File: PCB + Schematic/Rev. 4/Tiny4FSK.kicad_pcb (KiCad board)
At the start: 4 copper layers, 18.5 x 64 mm, 80 parts, among them IC1 SI4063, J1 SWD, J2 GPIO, J3 USBC, J4 USB, J5 I2C, J6 Power, J7 SPI, J8 USB, SW1 RST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

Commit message: Add ATGM336H, start snap-off boards
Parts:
- added C28: 10uF, Capacitor_SMD:C_0805_2012Metric_Pad1.18x1.45mm_HandSolder, F.Cu at (145.2, 56.2)
- added R14: 1M, Resistor_SMD:R_0805_2012Metric_Pad1.20x1.40mm_HandSolder, F.Cu at (146.0, 71.8)
- added R15: 1M, Resistor_SMD:R_0805_2012Metric_Pad1.20x1.40mm_HandSolder, F.Cu at (145.8, 74.8)
- U2: value MAX-M10S -> ATGM336H; footprint RF_GPS:ublox_MAX -> RF_GPS_Extended:ATGM336H
- moved R7 53.1 mm to (165.2, 54.1)
- moved R3 50.6 mm to (162.1, 55.0), turned to -90 degrees
- moved R5 49.8 mm to (164.9, 56.0)
- moved J5 48.1 mm to (162.8, 82.7)
- moved J8 45.9 mm to (162.9, 65.8), turned to 90 degrees
- moved C15 45.7 mm to (145.2, 60.2), turned to 90 degrees
- moved BT1 43.1 mm to (214.2, 41.5)
- moved U3 42.0 mm to (164.4, 60.0), turned to 180 degrees
- moved FB1 38.3 mm to (171.2, 61.5), turned to 90 degrees
- moved J3 34.1 mm to (166.5, 48.3), turned to 180 degrees
- moved J2 33.4 mm to (162.8, 71.2)
- moved J7 29.2 mm to (162.8, 94.2)
- moved G*** 28.8 mm to (109.2, 88.2)
- moved C5 24.4 mm to (169.6, 54.1)
- moved C6 23.8 mm to (171.8, 55.8), turned to 90 degrees
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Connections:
- BT1 pad +: BATT_SENSE -> +BATT
- C15 pad 1: BATT_SENSE -> +BATT
- J3 pad A6: D+ Ext -> D+
- J3 pad A7: D- Ext -> D-
- J3 pad B6: D+ Ext -> D+
- J3 pad B7: D- Ext -> D-
- J6 pad 1: BATT_SENSE -> +BATT
- J8 pad 1: D+ Ext -> D+
- J8 pad 2: D- Ext -> D-
- JP1 pad 2: BATT_SENSE -> +BATT
- R6 pad 1: SCL -> +3.3V
- R6 pad 2: +3.3V -> SCL
- SW2 pad 1: BATT_SENSE -> +BATT
- U2 pad 16: SDA -> unconnected-(U2-SDA-Pad16)
- U2 pad 17: SCL -> unconnected-(U2-SCL-Pad17)
- U2 pad 2: unconnected-(U2-TXD-Pad2) -> RXD
- U2 pad 3: unconnected-(U2-RXD-Pad3) -> TXD
- U2 pad 5: EXTINT -> Earth
- U2 pad 6: unconnected-(U2-V_BCKP-Pad6) -> +3.3V
- U2 pad 7: +3.3V -> unconnected-(U2-NC-Pad7)
- U2 pad 9: unconnected-(U2-~{RESET}-Pad9) -> Earth
- U4 pad 11: EXTINT -> unconnected-(U4-PA06-Pad11)
- U4 pad 15: unconnected-(U4-PA10-Pad15) -> TXD
- U4 pad 16: unconnected-(U4-PA11-Pad16) -> RXD
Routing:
- net D-: track 14.9 -> 58.9 mm, vias 0 -> 2
- net D+: track 15.8 -> 55.0 mm, vias 0 -> 1
- net A1: track 0.00 -> 23.8 mm, vias 0 -> 1
- net A2: track 0.00 -> 23.2 mm, vias 0 -> 1
- net Net-(J3-SHIELD): track 0.00 -> 19.5 mm
- net +BATT: track 0.00 -> 19.4 mm, vias 0 -> 1
- net D13: track 0.00 -> 18.0 mm, vias 0 -> 1
- net D12: track 0.00 -> 17.9 mm, vias 0 -> 1
- net USB: track 0.00 -> 9.59 mm
- net +3.3V: track 54.2 -> 47.7 mm
- net Net-(J3-CC1): track 0.00 -> 4.64 mm
- net BST_IN: track 10.9 -> 13.9 mm
- net Net-(J3-CC2): track 0.00 -> 2.65 mm
- net Earth: track 10.2 -> 12.7 mm, vias 6 -> 7
- net RF_SS: track 14.0 -> 16.3 mm
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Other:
- board size 18.5 x 64 mm -> 33 x 64 mm

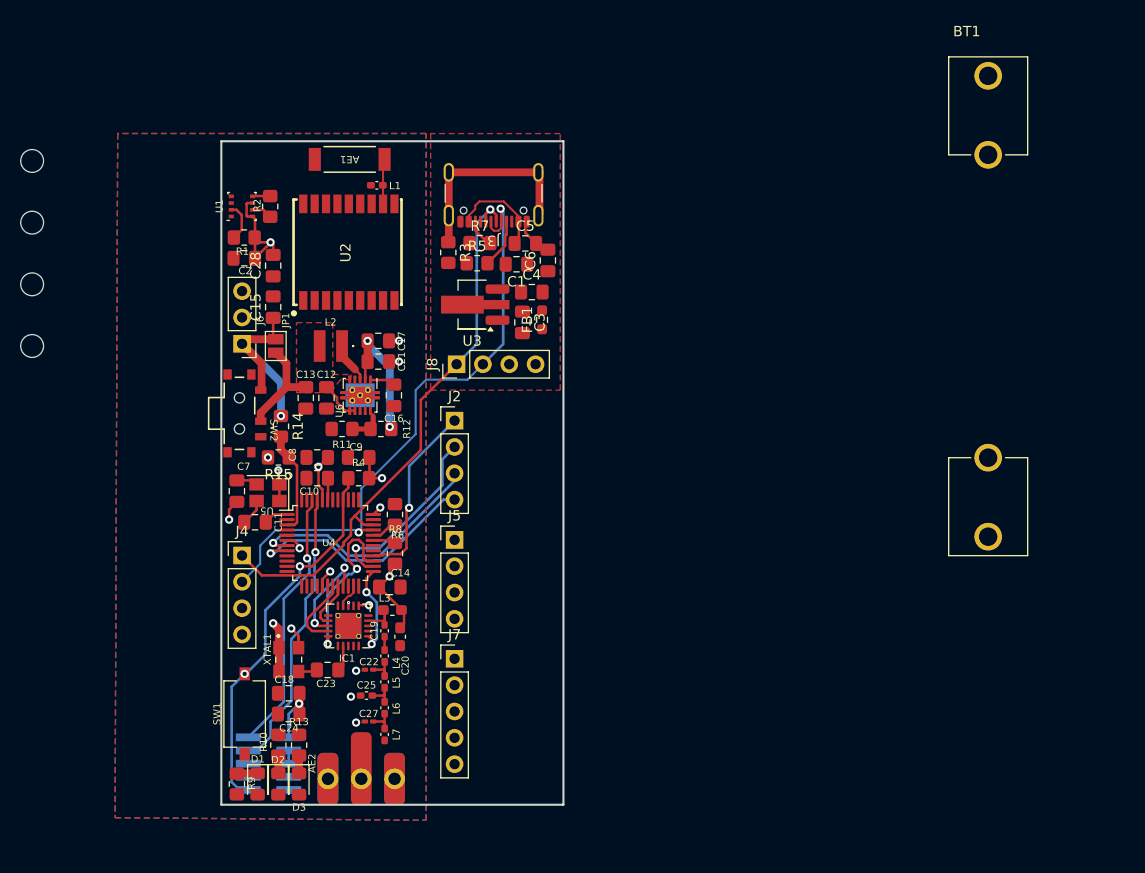
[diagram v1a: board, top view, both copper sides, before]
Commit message: USB Breakout, PCB further along
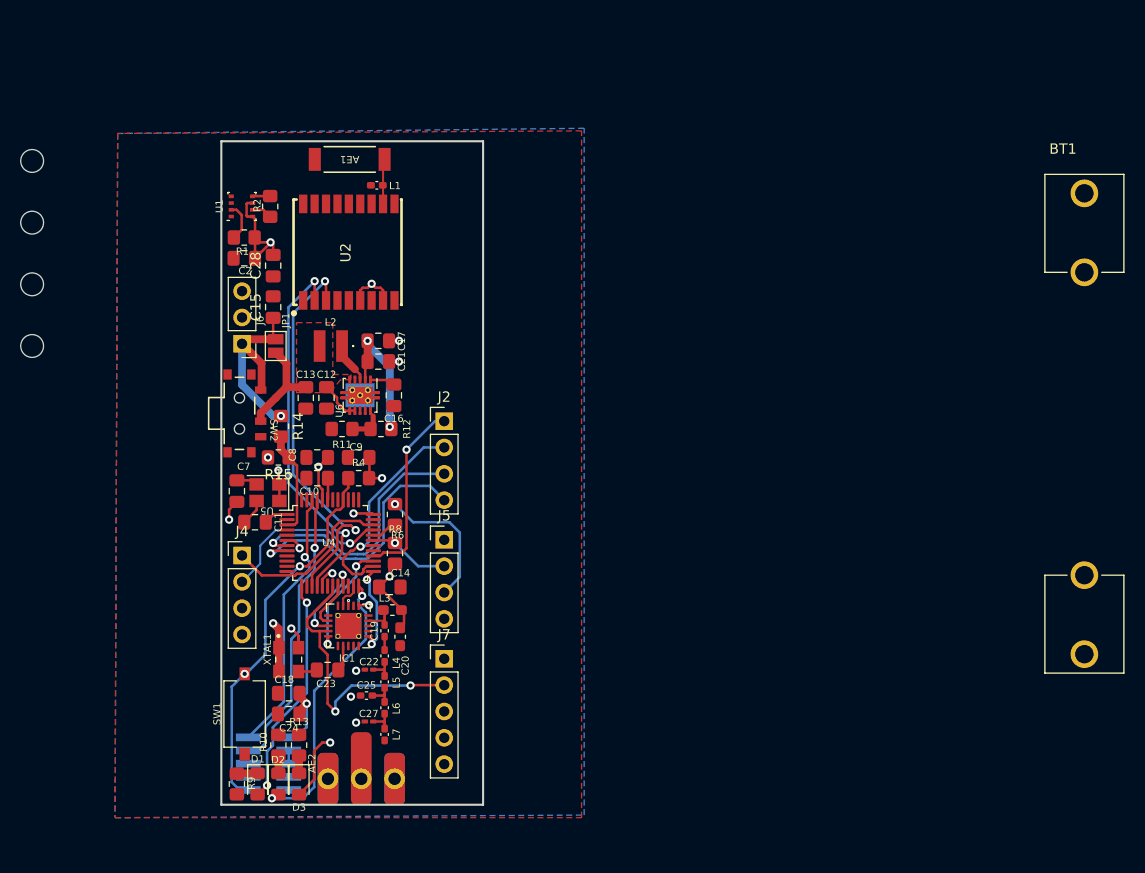
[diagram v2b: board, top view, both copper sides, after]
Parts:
- removed C1, C3: 1uF, Capacitor_SMD:C_0805_2012Metric_Pad1.18x1.45mm_HandSolder
- removed C4, C5: 100 nF, Capacitor_SMD:C_0805_2012Metric_Pad1.18x1.45mm_HandSolder
- removed C6: 4.5 nF, Capacitor_SMD:C_0805_2012Metric_Pad1.18x1.45mm_HandSolder
- removed FB1: BLM18AG121SN1D, Resistor_SMD:R_0603_1608Metric_Pad0.98x0.95mm_HandSolder
- removed J3: USBC, Connector_USB:USB_C_Receptacle_GCT_USB4105-xx-A_16P_TopMnt_Horizontal
- removed J8: USB, Connector_PinHeader_2.54mm:PinHeader_1x04_P2.54mm_Vertical
- removed R3: 1M, Resistor_SMD:R_0805_2012Metric_Pad1.20x1.40mm_HandSolder
- removed R5, R7: 5k1, Resistor_SMD:R_0805_2012Metric_Pad1.20x1.40mm_HandSolder
- removed U3: Linear Step-Down, Package_TO_SOT_SMD:SOT-89-3_Handsoldering
- moved BT1 14.6 mm to (223.5, 52.8)
- moved J2 1.00 mm to (161.8, 71.2)
- moved J5 1.00 mm to (161.8, 82.7)
- moved J7 1.00 mm to (161.8, 94.2)
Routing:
- net D-: track 58.9 -> 16.8 mm, vias 2 -> 1
- net TXD: track 0.00 -> 38.6 mm, vias 0 -> 2
- net D+: track 55.0 -> 16.8 mm, vias 1 -> 0
- net RXD: track 0.00 -> 36.2 mm, vias 0 -> 2
- net ERROR: track 0.00 -> 27.3 mm, vias 0 -> 2
- net SUCCESS: track 0.00 -> 22.3 mm, vias 0 -> 2
- net MOSI: track 7.12 -> 27.6 mm, vias 0 -> 2
- net Net-(J3-SHIELD): track 19.5 -> 0.00 mm
- net +3.3V: track 47.7 -> 61.7 mm, vias 13 -> 15
- net SCL: track 2.50 -> 16.3 mm, vias 0 -> 1
- net USB: track 9.59 -> 0.00 mm
- net SDA: track 2.19 -> 7.87 mm, vias 0 -> 1
- net RF_SS: track 16.3 -> 11.3 mm
- net Net-(J3-CC1): track 4.64 -> 0.00 mm
- net D13: track 18.0 -> 20.7 mm
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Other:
- board size 33 x 64 mm -> 25.2 x 64 mm

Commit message: Expansion GPIO
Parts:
- moved H4 75.9 mm to (181.0, 111.8)
- moved BT1 33.8 mm to (190.8, 61.3)
- moved G*** 21.5 mm to (93.6, 79.8)
- moved H1 20.3 mm to (142.2, 46.2)
- moved G*** 19.5 mm to (104.0, 79.8)
- moved G*** 15.0 mm to (110.8, 90.2)
- moved G*** 14.2 mm to (95.2, 90.5)
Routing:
- net SDA: track 7.87 -> 57.7 mm, vias 1 -> 2
- net SCL: track 16.3 -> 57.4 mm, vias 1 -> 3
- net SCK: track 4.61 -> 30.7 mm, vias 0 -> 1
- net MISO: track 8.32 -> 33.4 mm
- net GPIO1: track 0.00 -> 7.55 mm, vias 0 -> 2
- net +3.3V: track 61.7 -> 64.9 mm, vias 15 -> 14
- net MOSI: track 27.6 -> 30.6 mm
- net TXD: track 38.6 -> 35.8 mm
- net RF_SS: track 11.3 -> 13.9 mm
- net ERROR: track 27.3 -> 29.5 mm, vias 2 -> 4
- net RXD: track 36.2 -> 37.8 mm
- net Earth: track 10.2 -> 11.5 mm
- net D+: track 16.8 -> 18.1 mm
- net D13: track 20.7 -> 21.6 mm
- net D-: track 16.8 -> 16.1 mm

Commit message: USB Prog, updates
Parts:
- U5: footprint Oscillator_TCXO:ATXK-H11-E-32.768KHZ-E50-T3 -> Oscillator_TCXO:KDS-1XZA032768AD19
- moved H4 14.6 mm to (169.0, 103.5)
- moved C7 0.78 mm to (141.4, 77.3)
- moved IC1 0.50 mm to (152.5, 91.5)
- moved C28 0.21 mm to (145.4, 56.4)
- turned U5 to 180 degrees
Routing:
- net RF_RST: track 0.00 -> 23.5 mm, vias 0 -> 2
- net Earth: track 11.5 -> 19.6 mm, vias 7 -> 16
- net Net-(AE2-RF): track 0.00 -> 4.96 mm
- net +3.3V: track 64.9 -> 67.5 mm
- net SDN: track 8.73 -> 9.97 mm
- net RF_SS: track 13.9 -> 12.7 mm
- net GPIO1: track 7.55 -> 6.56 mm
- net SWDIO: track 25.8 -> 26.7 mm
- net MISO: track 33.4 -> 32.7 mm
- net D-: track 16.1 -> 16.7 mm
- net A1: track 24.2 -> 24.8 mm
- net A2: track 25.1 -> 25.7 mm
- net ERROR: track 29.5 -> 28.9 mm
- net Net-(IC1-XIN): track 2.50 -> 2.00 mm

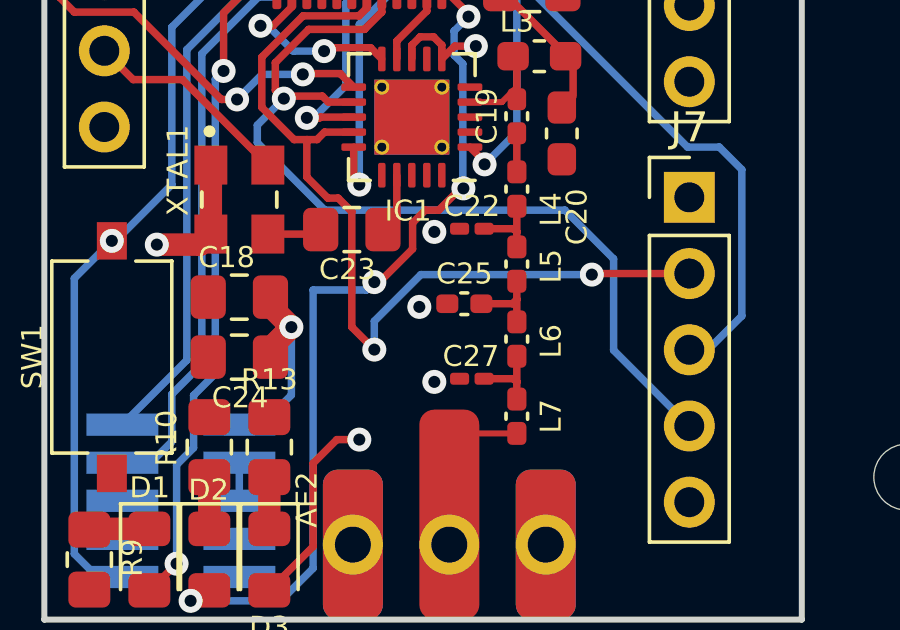
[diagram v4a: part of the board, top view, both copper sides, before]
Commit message: 0402s for JLCPCB capabilities
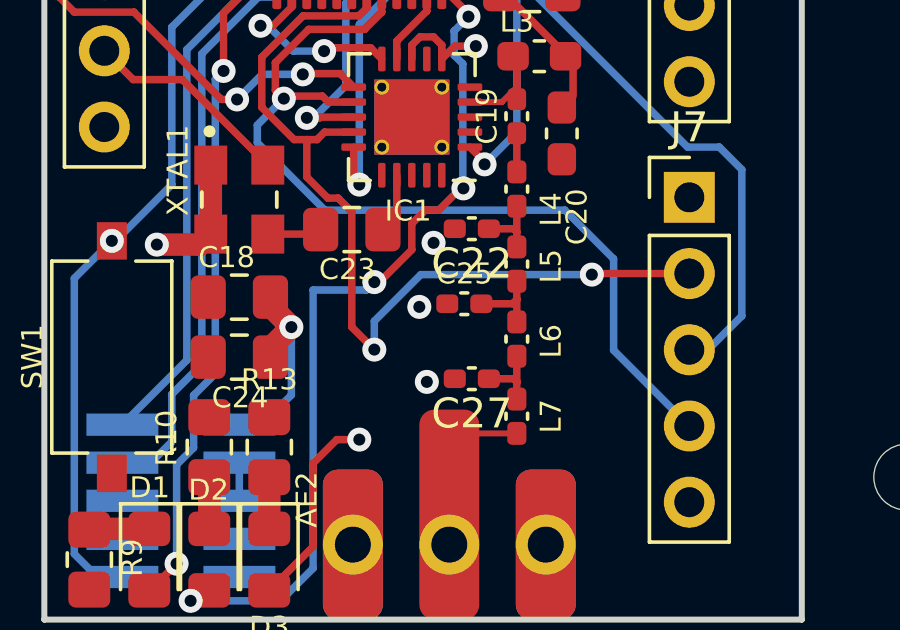
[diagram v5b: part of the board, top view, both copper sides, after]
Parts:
- C22, C27: footprint Capacitor_SMD:C_0201_0603Metric_Pad0.64x0.40mm_HandSolder -> Capacitor_SMD:C_0402_1005Metric_Pad0.74x0.62mm_HandSolder
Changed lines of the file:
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@@
 			)
 		)
+		(sheetname "Root")
+		(sheetfile "Tiny4FSK.kicad_sch")
 		(fp_line
 			(start 2.032 1.651)
@@
 		)
 	)
-	(footprint "Capacitor_SMD:C_0201_0603Metric_Pad0.64x0.40mm_HandSolder"
+	(footprint "Capacitor_SMD:C_0402_1005Metric_Pad0.74x0.62mm_HandSolder"
 		(layer "F.Cu")
 		(at 154.5 95.22125 180)
-		(descr "Capacitor SMD 0201 (0603 Metric), square (rectangular) end terminal, IPC_7351 nominal with elongated pad for handsoldering. (Body size source: https://www.vishay.com/docs/20052/crcw0201e3.pdf), generated with kicad-footprint-generator")
+		(descr "Capacitor SMD 0402 (1005 Metric), square (rectangular) end terminal, IPC_7351 nominal with elongated pad for handsoldering. (Body size source: IPC-SM-782 page 76, https://www.pcb-3d.com/wordpress/wp-content/uploads/ipc-sm-782a_amendment_1_and_2.pdf), generated with kicad-footprint-generator")
 		(tags "capacitor handsolder")
 		(property "Reference" "C22"
-			(at 0 0.75 180)
+			(at 0 -1.16 180)
 			(layer "F.SilkS")
 			(effects
 				(font
-					(size 0.7 0.7)
-					(thickness 0.1)
+					(size 1 1)
+					(thickness 0.15)
 				)
 			)
 		)
 		(property "Value" "15 pF"
-			(at 0 1.05 180)
+			(at 0 1.16 180)
 			(layer "F.Fab")
 			(effects
@@
 			)
 		)
-		(property "Footprint" "Capacitor_SMD:C_0201_0603Metric_Pad0.64x0.40mm_HandSolder"
+		(property "Footprint" "Capacitor_SMD:C_0402_1005Metric_Pad0.74x0.62mm_HandSolder"
 			(at 0 0 180)
 			(unlocked yes)
@@
 		(sheetname "Root")
 		(sheetfile "Tiny4FSK.kicad_sch")
-		(clearance 0.01)
 		(attr smd)
 		(fp_line
-			(start 0.88 0.35)
-			(end -0.88 0.35)
+			(start -0.115835 0.36)
+			(end 0.115835 0.36)
+			(stroke
+				(width 0.12)
+				(type solid)
+			)
+			(layer "F.SilkS")
+		)
+		(fp_line
+			(start -0.115835 -0.36)
+			(end 0.115835 -0.36)
+			(stroke
+				(width 0.12)
+				(type solid)
+			)
+			(layer "F.SilkS")
+		)
+		(fp_line
+			(start 1.08 0.46)
+			(end -1.08 0.46)
 			(stroke
 				(width 0.05)
@@
 		)
 		(fp_line
-			(start 0.88 -0.35)
-			(end 0.88 0.35)
+			(start 1.08 -0.46)
+			(end 1.08 0.46)
 			(stroke
 				(width 0.05)
@@
 		)
 		(fp_line
-			(start -0.88 0.35)
-			(end -0.88 -0.35)
+			(start -1.08 0.46)
+			(end -1.08 -0.46)
 			(stroke
 				(width 0.05)
@@
 		)
 		(fp_line
-			(start -0.88 -0.35)
-			(end 0.88 -0.35)
+			(start -1.08 -0.46)
+			(end 1.08 -0.46)
 			(stroke
 				(width 0.05)
@@
 		)
 		(fp_line
-			(start 0.3 0.15)
-			(end -0.3 0.15)
+			(start 0.5 0.25)
+			(end -0.5 0.25)
 			(stroke
 				(width 0.1)
@@
 		)
 		(fp_line
-			(start 0.3 -0.15)
-			(end 0.3 0.15)
+			(start 0.5 -0.25)
+			(end 0.5 0.25)
 			(stroke
 				(width 0.1)
@@
 		)
 		(fp_line
-			(start -0.3 0.15)
-			(end -0.3 -0.15)
+			(start -0.5 0.25)
+			(end -0.5 -0.25)
 			(stroke
 				(width 0.1)
@@
 		)
 		(fp_line
-			(start -0.3 -0.15)
-			(end 0.3 -0.15)
+			(start -0.5 -0.25)
+			(end 0.5 -0.25)
 			(stroke
 				(width 0.1)
@@
 		)
 		(fp_text user "${REFERENCE}"
-			(at 0 -0.68 180)
+			(at 0 0 180)
 			(layer "F.Fab")
 			(effects
@@
 			)
 		)
-		(pad "" smd roundrect
-			(at -0.4325 0 180)
-			(size 0.458 0.36)
-			(layers "F.Paste")
-			(roundrect_rratio 0.25)
-		)
-		(pad "" smd roundrect
-			(at 0.4325 0 180)
-			(size 0.458 0.36)
-			(layers "F.Paste")
-			(roundrect_rratio 0.25)
-		)
 		(pad "1" smd roundrect
-			(at -0.4075 0 180)
-			(size 0.635 0.4)
-			(layers "F.Cu" "F.Mask")
+			(at -0.5675 0 180)
+			(size 0.735 0.62)
+			(layers "F.Cu" "F.Paste" "F.Mask")
 			(roundrect_rratio 0.25)
 			(net 47 "Net-(C22-Pad1)")
@@
 		)
 		(pad "2" smd roundrect
-			(at 0.4075 0 180)
-			(size 0.635 0.4)
-			(layers "F.Cu" "F.Mask")
+			(at 0.5675 0 180)
+			(size 0.735 0.62)
+			(layers "F.Cu" "F.Paste" "F.Mask")
 			(roundrect_rratio 0.25)
 			(net 1 "Earth")
 			(pintype "passive")
 		)
-		(model "${KICAD6_3DMODEL_DIR}/Capacitor_SMD.3dshapes/C_0201_0603Metric.wrl"
+		(model "${KICAD8_3DMODEL_DIR}/Capacitor_SMD.3dshapes/C_0402_1005Metric.wrl"
 			(offset
 				(xyz 0 0 0)
@@
 		)
 	)
-	(footprint "Capacitor_SMD:C_0201_0603Metric_Pad0.64x0.40mm_HandSolder"
+	(footprint "Capacitor_SMD:C_0402_1005Metric_Pad0.74x0.62mm_HandSolder"
 		(layer "F.Cu")
 		(at 154.5 100.22125 180)
-		(descr "Capacitor SMD 0201 (0603 Metric), square (rectangular) end terminal, IPC_7351 nominal with elongated pad for handsoldering. (Body size source: https://www.vishay.com/docs/20052/crcw0201e3.pdf), generated with kicad-footprint-generator")
+		(descr "Capacitor SMD 0402 (1005 Metric), square (rectangular) end terminal, IPC_7351 nominal with elongated pad for handsoldering. (Body size source: IPC-SM-782 page 76, https://www.pcb-3d.com/wordpress/wp-content/uploads/ipc-sm-782a_amendment_1_and_2.pdf), generated with kicad-footprint-generator")
 		(tags "capacitor handsolder")
 		(property "Reference" "C27"
-			(at 0.029752 0.75 180)
+			(at 0 -1.16 180)
 			(layer "F.SilkS")
 			(effects
 				(font
-					(size 0.7 0.7)
-					(thickness 0.1)
+					(size 1 1)
+					(thickness 0.15)
 				)
 			)
 		)
 		(property "Value" "10 pF"
-			(at 0 1.05 180)
+			(at 0 1.16 180)
 			(layer "F.Fab")
 			(effects
@@
 			)
 		)
-		(property "Footprint" "Capacitor_SMD:C_0201_0603Metric_Pad0.64x0.40mm_HandSolder"
+		(property "Footprint" "Capacitor_SMD:C_0402_1005Metric_Pad0.74x0.62mm_HandSolder"
 			(at 0 0 180)
 			(unlocked yes)
@@
 		(sheetname "Root")
 		(sheetfile "Tiny4FSK.kicad_sch")
-		(clearance 0.1)
 		(attr smd)
 		(fp_line
-			(start 0.88 0.35)
-			(end -0.88 0.35)
+			(start -0.115835 0.36)
+			(end 0.115835 0.36)
+			(stroke
+				(width 0.12)
+				(type solid)
+			)
+			(layer "F.SilkS")
+		)
+		(fp_line
+			(start -0.115835 -0.36)
+			(end 0.115835 -0.36)
+			(stroke
+				(width 0.12)
+				(type solid)
+			)
+			(layer "F.SilkS")
+		)
+		(fp_line
+			(start 1.08 0.46)
+			(end -1.08 0.46)
 			(stroke
 				(width 0.05)
@@
 		)
 		(fp_line
-			(start 0.88 -0.35)
-			(end 0.88 0.35)
+			(start 1.08 -0.46)
+			(end 1.08 0.46)
 			(stroke
 				(width 0.05)
@@
 		)
 		(fp_line
-			(start -0.88 0.35)
-			(end -0.88 -0.35)
+			(start -1.08 0.46)
+			(end -1.08 -0.46)
 			(stroke
 				(width 0.05)
@@
 		)
 		(fp_line
-			(start -0.88 -0.35)
-			(end 0.88 -0.35)
+			(start -1.08 -0.46)
+			(end 1.08 -0.46)
 			(stroke
 				(width 0.05)
@@
 		)
 		(fp_line
-			(start 0.3 0.15)
-			(end -0.3 0.15)
+			(start 0.5 0.25)
+			(end -0.5 0.25)
 			(stroke
 				(width 0.1)
@@
 		)
 		(fp_line
-			(start 0.3 -0.15)
-			(end 0.3 0.15)
+			(start 0.5 -0.25)
+			(end 0.5 0.25)
 			(stroke
 				(width 0.1)
@@
 		)
 		(fp_line
-			(start -0.3 0.15)
-			(end -0.3 -0.15)
+			(start -0.5 0.25)
+			(end -0.5 -0.25)
 			(stroke
 				(width 0.1)
@@
 		)
 		(fp_line
-			(start -0.3 -0.15)
-			(end 0.3 -0.15)
+			(start -0.5 -0.25)
+			(end 0.5 -0.25)
 			(stroke
 				(width 0.1)
@@
 		)
 		(fp_text user "${REFERENCE}"
-			(at 0 -0.68 180)
+			(at 0 0 180)
 			(layer "F.Fab")
 			(effects
@@
 			)
 		)
-		(pad "" smd roundrect
-			(at -0.4325 0 180)
-			(size 0.458 0.36)
-			(layers "F.Paste")
-			(roundrect_rratio 0.25)
-		)
-		(pad "" smd roundrect
-			(at 0.4325 0 180)
-			(size 0.458 0.36)
-			(layers "F.Paste")
-			(roundrect_rratio 0.25)
-		)
 		(pad "1" smd roundrect
-			(at -0.4075 0 180)
-			(size 0.635 0.4)
-			(layers "F.Cu" "F.Mask")
+			(at -0.5675 0 180)
+			(size 0.735 0.62)
+			(layers "F.Cu" "F.Paste" "F.Mask")
 			(roundrect_rratio 0.25)
 			(net 50 "Net-(C27-Pad1)")
@@
 		)
 		(pad "2" smd roundrect
-			(at 0.4075 0 180)
-			(size 0.635 0.4)
-			(layers "F.Cu" "F.Mask")
+			(at 0.5675 0 180)
+			(size 0.735 0.62)
+			(layers "F.Cu" "F.Paste" "F.Mask")
 			(roundrect_rratio 0.25)
 			(net 1 "Earth")
 			(pintype "passive")
 		)
-		(model "${KICAD6_3DMODEL_DIR}/Capacitor_SMD.3dshapes/C_0201_0603Metric.wrl"
+		(model "${KICAD8_3DMODEL_DIR}/Capacitor_SMD.3dshapes/C_0402_1005Metric.wrl"
 			(offset
 				(xyz 0 0 0)
@@
 	)
 	(via
-		(at 153.25 100.32625)
+		(at 153 100.32625)
 		(size 0.8)
 		(drill 0.4)
@@
 	)
 	(via
-		(at 153.25 95.32625)
+		(at 153.225 95.691497)
 		(size 0.8)
 		(drill 0.4)
@@
 	)
 	(segment
-		(start 153.39875 94.60125)
-		(end 152.949695 94.60125)
+		(start 152.949695 94.60125)
+		(end 152.5 95.050945)
 		(width 0.25)
 		(layer "F.Cu")
@@
 	)
 	(segment
-		(start 152.525 95.8951)
-		(end 151.4201 97)
+		(start 145.475 107.275)
+		(end 145.125735 107.624265)
 		(width 0.25)
 		(layer "F.Cu")
@@
 	)
 	(segment
-		(start 145.475 107.275)
-		(end 145.125735 107.624265)
+		(start 151.4201 97)
+		(end 151.25 97)
+		(width 0.25)
+		(layer "F.Cu")
+		(net 38)
+	)
+	(segment
+		(start 154.123566 93.876434)
+		(end 153.39875 94.60125)
 		(width 0.25)
 		(layer "F.Cu")
@@
 	)
 	(segment
-		(start 154.123566 93.876434)
-		(end 153.39875 94.60125)
+		(start 153.39875 94.60125)
+		(end 152.949695 94.60125)
 		(width 0.25)
 		(layer "F.Cu")
@@
 	)
 	(segment
-		(start 151.4201 97)
-		(end 151.25 97)
+		(start 152.5 95.050945)
+		(end 152.5 95.9201)
 		(width 0.25)
 		(layer "F.Cu")
@@
 	)
 	(segment
-		(start 152.949695 94.60125)
-		(end 152.525 95.025945)
+		(start 152.5 95.9201)
+		(end 151.4201 97)
 		(width 0.25)
 		(layer "F.Cu")
@@
 		(width 0.25)
 		(layer "F.Cu")
-		(net 38)
-	)
-	(segment
-		(start 152.525 95.025945)
-		(end 152.525 95.8951)
-		(width 0.25)
-		(layer "F.Cu")
